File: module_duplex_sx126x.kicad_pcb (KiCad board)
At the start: 4 copper layers, 55.4 x 45.7 mm, 34 parts, among them J1 USB_B_Mini, J2 Conn_01x08_Pin, J3 Conn_01x05, J4 Conn_01x04, J6 Conn_01x02, SW1 SW_Push, U1 STM32F103C8Tx, U2 AMS1117-3.3, U3 SN65HVD230, U4 Ai-Thinker-Ra-02, U5 Ai-Thinker-Ra-02, Y1 16M, Y2 32.768k

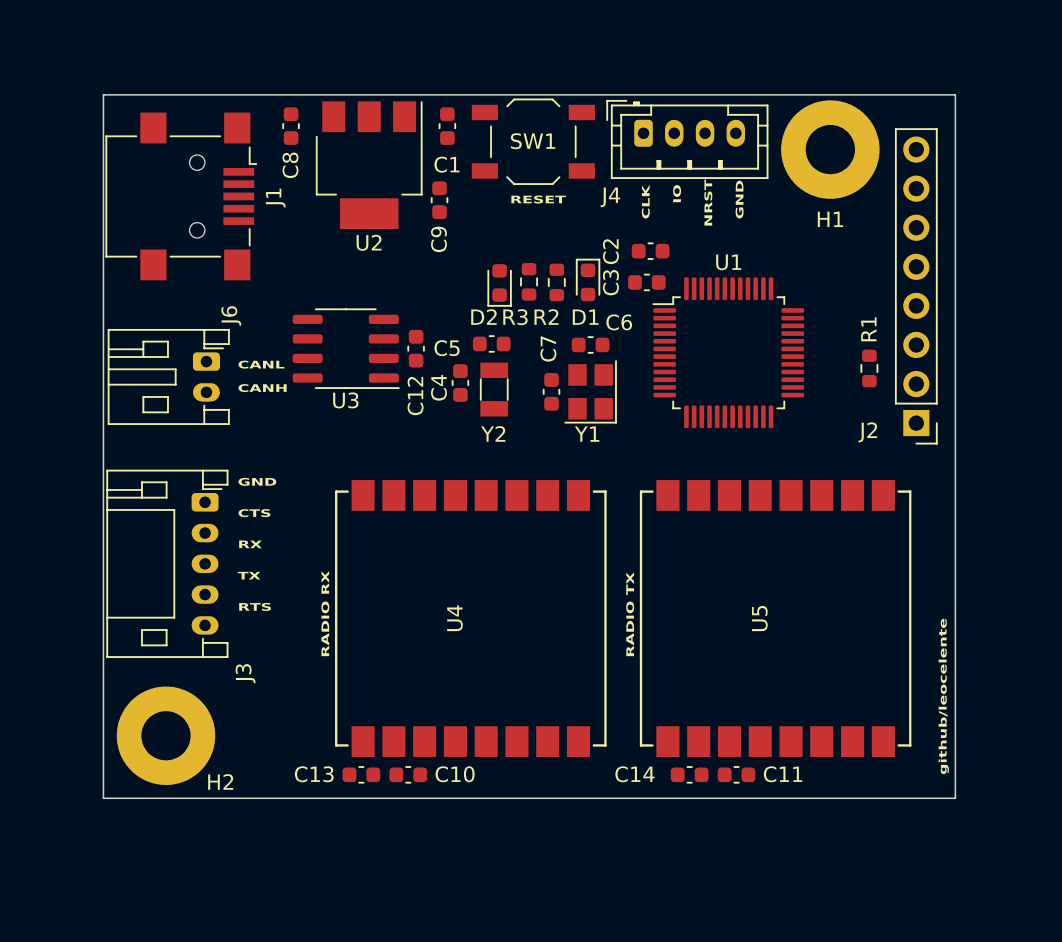
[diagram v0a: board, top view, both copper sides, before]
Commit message: Reduced expansion pins by simplifying select function with pull up/down
Signed-off-by: Leonardo Celente <leocelente@gmail.com>
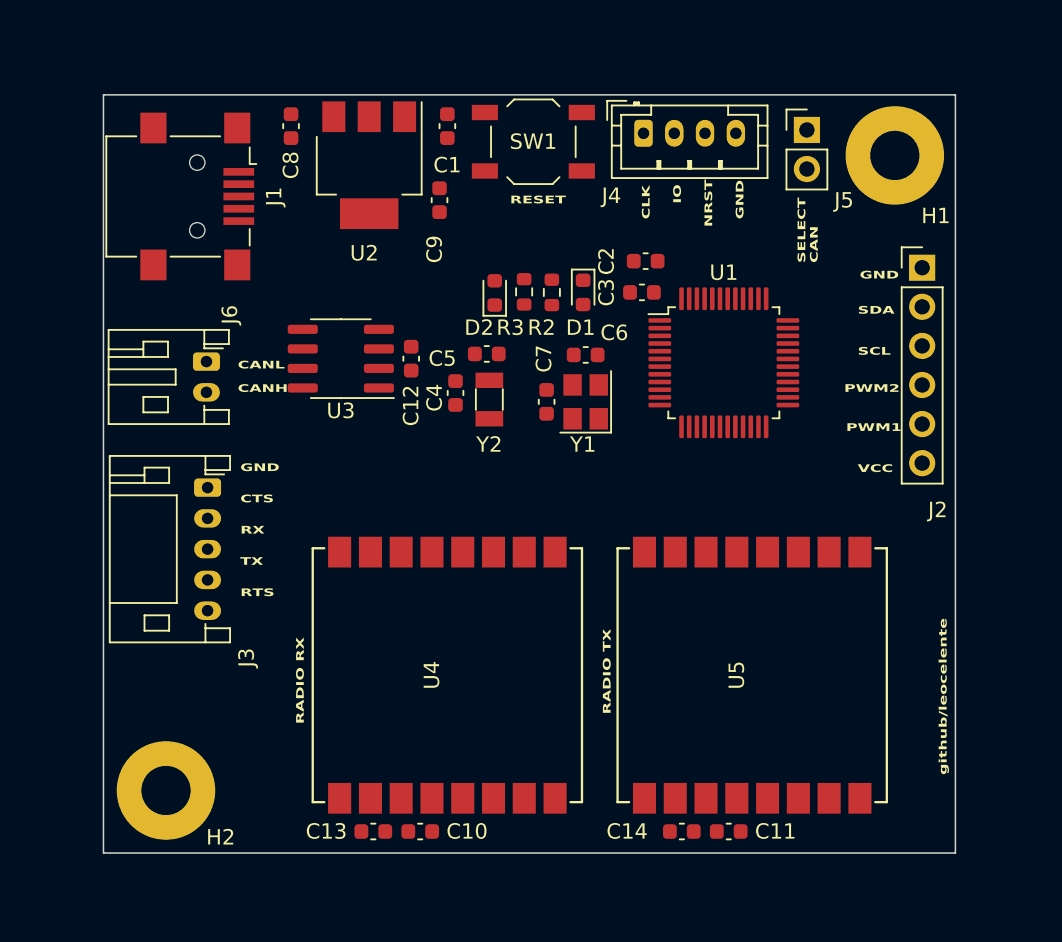
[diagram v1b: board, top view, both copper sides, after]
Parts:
- removed R1: 10k, Resistor_SMD:R_0603_1608Metric
- added J5: Conn_01x02_Pin, Connector_PinHeader_2.54mm:PinHeader_1x02_P2.54mm_Vertical, F.Cu at (108.7, 47.0)
- J2: value Conn_01x08_Pin -> Conn_01x06_Pin; footprint Connector_PinHeader_2.54mm:PinHeader_1x08_P2.54mm_Vertical -> Connector_PinHeader_2.54mm:PinHeader_1x06_P2.54mm_Vertical
- moved J2 10.1 mm to (116.2, 55.9), turned to 0 degrees
- moved H1 4.21 mm to (114.4, 48.6)
- moved U4 3.99 mm to (85.3, 82.4)
- moved U5 3.99 mm to (105.2, 82.4)
- moved C13 3.76 mm to (80.5, 92.6)
- moved C10 3.76 mm to (83.6, 92.6)
- moved C11 3.72 mm to (103.6, 92.6)
- moved C14 3.72 mm to (100.6, 92.6)
- moved H2 3.56 mm to (67.1, 89.9)
- moved J3 0.97 mm to (69.8, 70.2)
- moved C7 0.72 mm to (91.8, 64.7)
- moved Y1 0.72 mm to (94.3, 64.7)
- moved C2 0.72 mm to (98.2, 55.5)
- moved C5 0.72 mm to (87.9, 61.5)
- moved R3 0.72 mm to (90.3, 57.5)
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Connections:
- J2 pad 2: Net-(J2-Pin_2) -> /I2C_SDA
- J2 pad 3: VCC -> /I2C_SCL
- J2 pad 4: /I2C_SDA -> /PWM_2
- J2 pad 5: /I2C_SCL -> /PWM_1
- J2 pad 6: /PWM_2 -> VCC
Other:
- board size 55.4 x 45.7 mm -> 55.4 x 49.3 mm
- board text added: "PWM1"
- board text added: "PWM2"
- board text added: "SCL"
- board text added: "SDA"
- board text added: "SELECT CAN"
- board text added: "VCC"

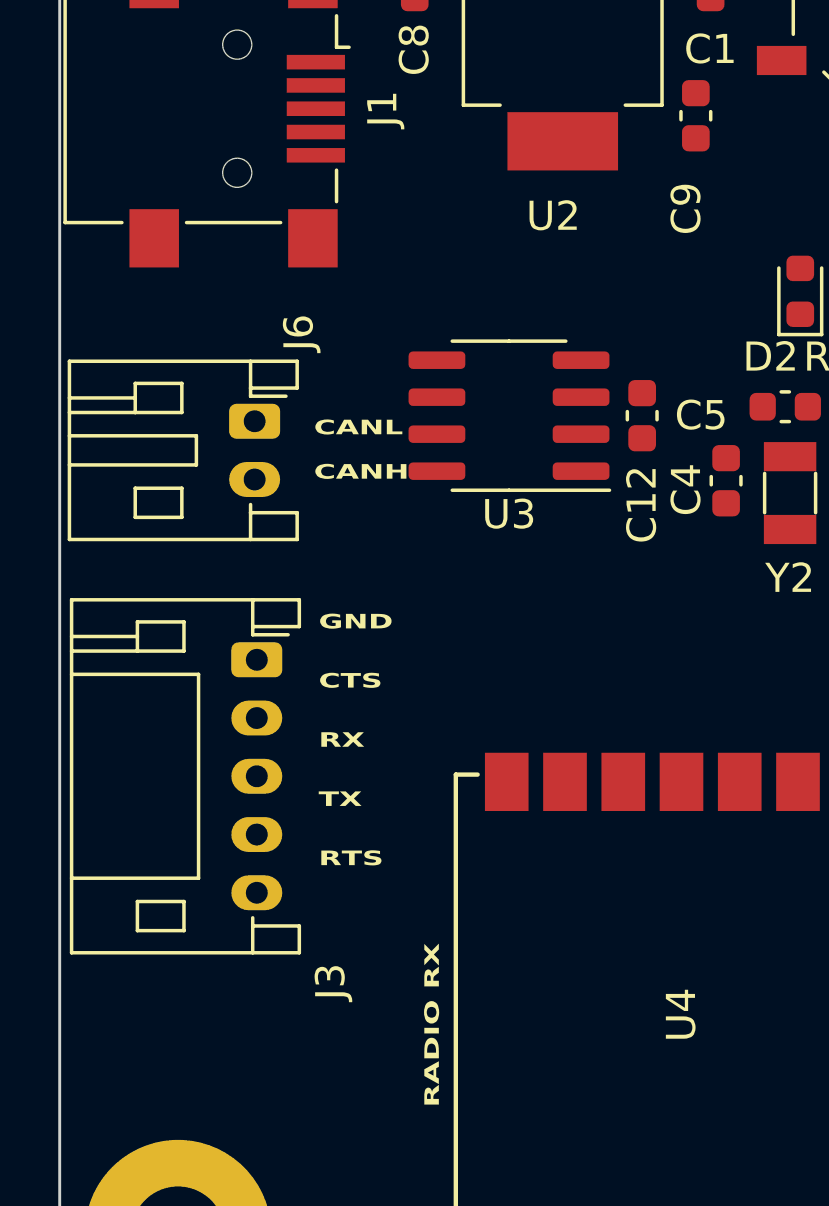
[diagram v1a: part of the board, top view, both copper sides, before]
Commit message: Added USB resistors
Signed-off-by: Leonardo Celente <leocelente@gmail.com>
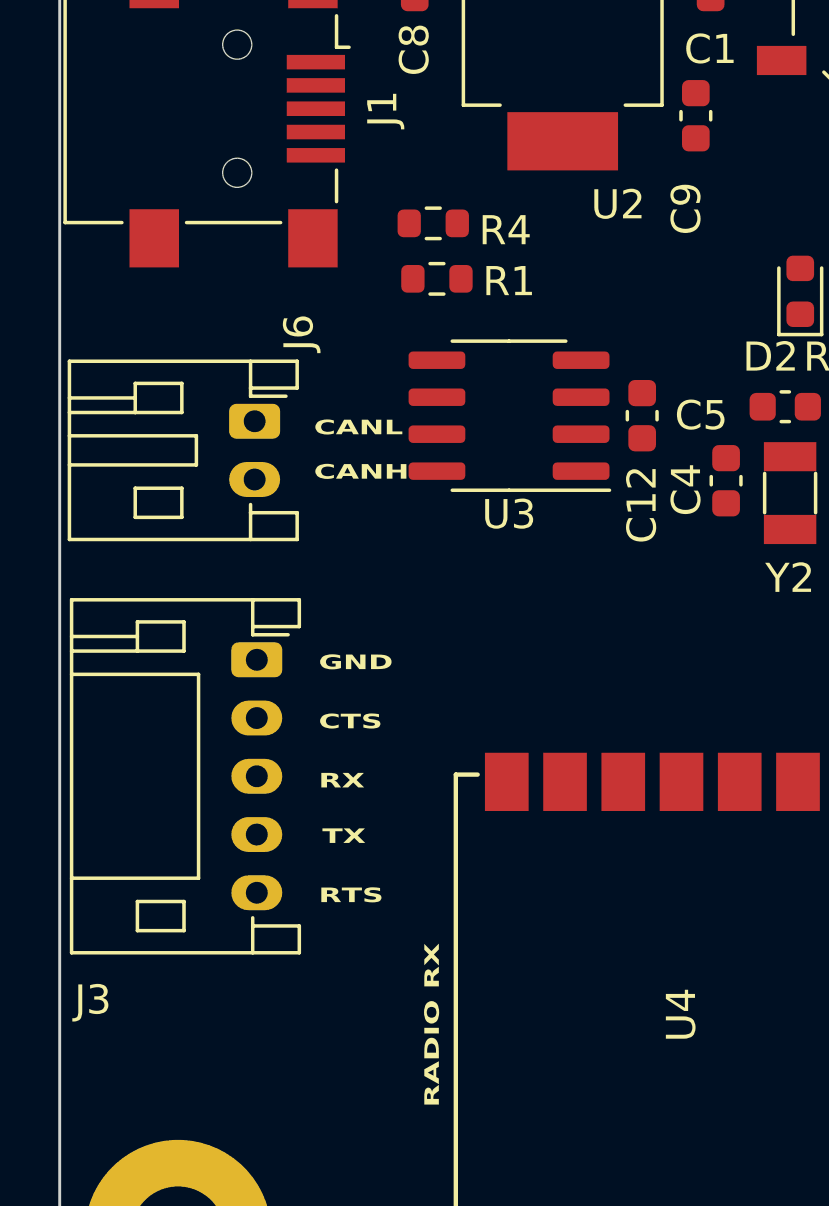
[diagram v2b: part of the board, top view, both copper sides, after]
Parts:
- added R1: 22, Resistor_SMD:R_0603_1608Metric, F.Cu at (75.9, 57.1)
- added R4: 22, Resistor_SMD:R_0603_1608Metric, F.Cu at (75.8, 55.2)
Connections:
- J1 pad 2: /USB_DM -> Net-(J1-D-)
- J1 pad 3: /USB_DP -> Net-(J1-D+)

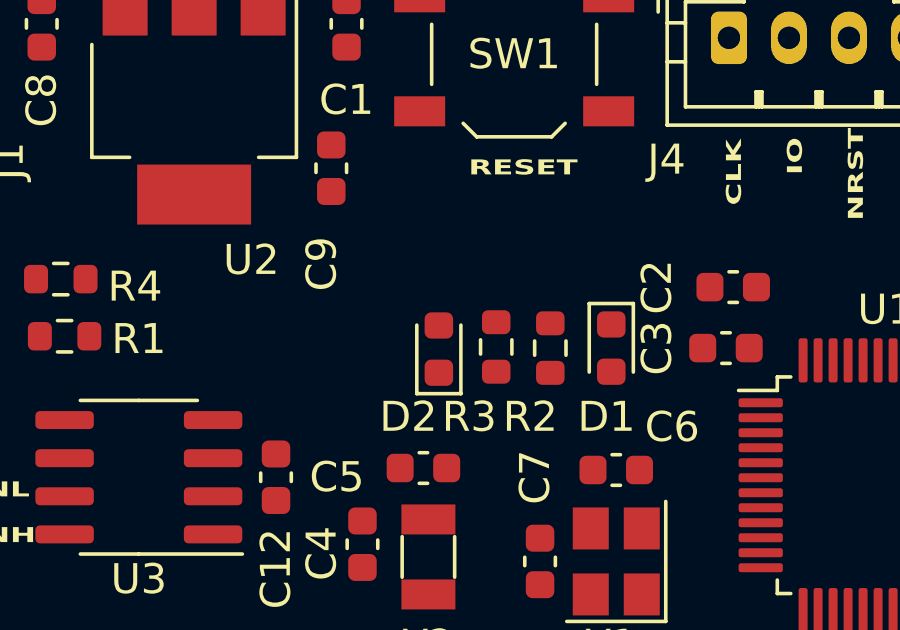
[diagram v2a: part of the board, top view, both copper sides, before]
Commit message: Added power indicator LED
Signed-off-by: Leonardo Celente <leocelente@gmail.com>
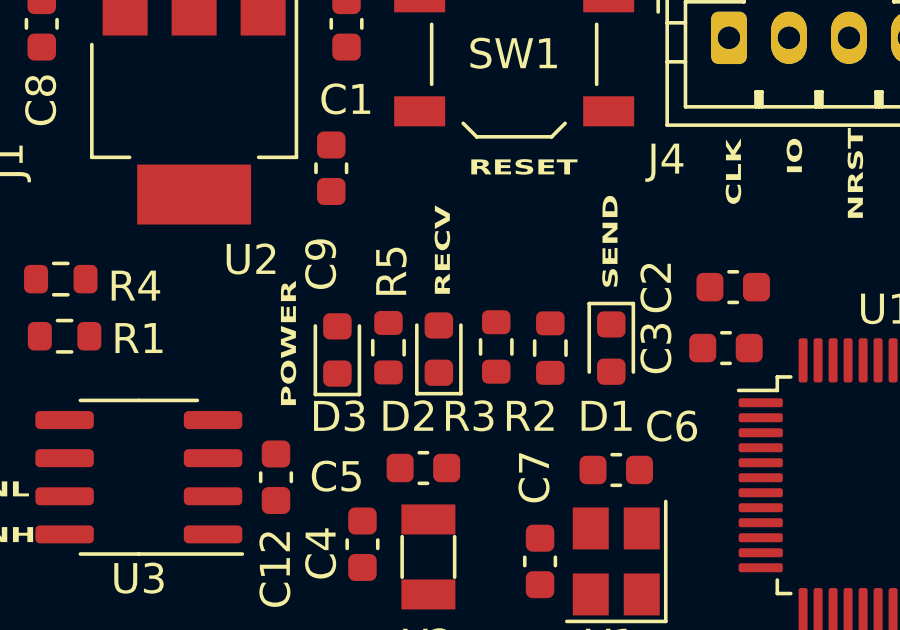
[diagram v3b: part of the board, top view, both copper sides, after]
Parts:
- added D3: LED, LED_SMD:LED_0603_1608Metric, F.Cu at (85.0, 57.6)
- added R5: 330, Resistor_SMD:R_0603_1608Metric, F.Cu at (86.7, 57.5)
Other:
- board text added: "POWER"
- board text added: "RECV"
- board text added: "SEND"
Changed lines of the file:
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@@
   (net 57 "Net-(D2-K)")
   (net 58 "Net-(J1-D+)")
+  (net 59 "Net-(D3-K)")
   (footprint "Connector_JST:JST_PH_S2B-PH-K_1x02_P2.00mm_Horizontal" (layer "F.Cu")
     (at 69.686 62.04 -90)
@@
     (pad "2" smd roundrect (at 0.825 0 90) (size 0.8 0.95) (layers "F.Cu" "F.Paste" "F.Mask") (roundrect_rratio 0.25)
       (net 42 "/RECV_LED") (pintype "passive"))
+    (model "${KICAD6_3DMODEL_DIR}/Resistor_SMD.3dshapes/R_0603_1608Metric.wrl"
+      (offset (xyz 0 0 0))
+      (scale (xyz 1 1 1))
+      (rotate (xyz 0 0 0))
+    )
+  )
+  (footprint "Resistor_SMD:R_0603_1608Metric" (layer "F.Cu")
+    (at 86.741 57.531 90)
+    (descr "Resistor SMD 0603 (1608 Metric), square (rectangular) end terminal, IPC_7351 nominal, (Body size source: IPC-SM-782 page 72, https://www.pcb-3d.com/wordpress/wp-content/uploads/ipc-sm-782a_amendment_1_and_2.pdf), generated with kicad-footprint-generator")
+    (tags "resistor")
+    (property "Sheetfile" "module_duplex_sx126x.kicad_sch")
+    (property "Sheetname" "")
+    (property "ki_description" "Resistor")
+    (property "ki_keywords" "R res resistor")
+    (attr smd)
+    (fp_text reference "R5" (at 2.54 0.127 90) (layer "F.SilkS")
+        (effects (font (size 1 1) (thickness 0.15)))
+    )
+    (fp_text value "330" (at 0 1.43 90) (layer "F.Fab")
+        (effects (font (size 1 1) (thickness 0.15)))
+    )
+    (fp_text user "${REFERENCE}" (at 0 0 90) (layer "F.Fab")
+        (effects (font (size 0.4 0.4) (thickness 0.06)))
+    )
+    (fp_line (start -0.237258 -0.5225) (end 0.237258 -0.5225)
+      (stroke (width 0.12) (type solid)) (layer "F.SilkS"))
+    (fp_line (start -0.237258 0.5225) (end 0.237258 0.5225)
+      (stroke (width 0.12) (type solid)) (layer "F.SilkS"))
+    (fp_line (start -1.48 -0.73) (end 1.48 -0.73)
+      (stroke (width 0.05) (type solid)) (layer "F.CrtYd"))
+    (fp_line (start -1.48 0.73) (end -1.48 -0.73)
+      (stroke (width 0.05) (type solid)) (layer "F.CrtYd"))
+    (fp_line (start 1.48 -0.73) (end 1.48 0.73)
+      (stroke (width 0.05) (type solid)) (layer "F.CrtYd"))
+    (fp_line (start 1.48 0.73) (end -1.48 0.73)
+      (stroke (width 0.05) (type solid)) (layer "F.CrtYd"))
+    (fp_line (start -0.8 -0.4125) (end 0.8 -0.4125)
+      (stroke (width 0.1) (type solid)) (layer "F.Fab"))
+    (fp_line (start -0.8 0.4125) (end -0.8 -0.4125)
+      (stroke (width 0.1) (type solid)) (layer "F.Fab"))
+    (fp_line (start 0.8 -0.4125) (end 0.8 0.4125)
+      (stroke (width 0.1) (type solid)) (layer "F.Fab"))
+    (fp_line (start 0.8 0.4125) (end -0.8 0.4125)
+      (stroke (width 0.1) (type solid)) (layer "F.Fab"))
+    (pad "1" smd roundrect (at -0.825 0 90) (size 0.8 0.95) (layers "F.Cu" "F.Paste" "F.Mask") (roundrect_rratio 0.25)
+      (net 59 "Net-(D3-K)") (pintype "passive"))
+    (pad "2" smd roundrect (at 0.825 0 90) (size 0.8 0.95) (layers "F.Cu" "F.Paste" "F.Mask") (roundrect_rratio 0.25)
+      (net 1 "GND") (pintype "passive"))
     (model "${KICAD6_3DMODEL_DIR}/Resistor_SMD.3dshapes/R_0603_1608Metric.wrl"
       (offset (xyz 0 0 0))
@@
       (net 12 "unconnected-(J1-Shield-Pad6)") (pinfunction "Shield") (pintype "passive+no_connect"))
     (model "${KICAD6_3DMODEL_DIR}/Connector_USB.3dshapes/USB_Mini-B_Lumberg_2486_01_Horizontal.wrl"
+      (offset (xyz 0 0 0))
+      (scale (xyz 1 1 1))
+      (rotate (xyz 0 0 0))
+    )
+  )
+  (footprint "LED_SMD:LED_0603_1608Metric" (layer "F.Cu")
+    (at 85.0392 57.6072 90)
+    (descr "LED SMD 0603 (1608 Metric), square (rectangular) end terminal, IPC_7351 nominal, (Body size source: http://www.tortai-tech.com/upload/download/2011102023233369053.pdf), generated with kicad-footprint-generator")
+    (tags "LED")
+    (property "Sheetfile" "module_duplex_sx126x.kicad_sch")
+    (property "Sheetname" "")
+    (property "ki_description" "Light emitting diode")
+    (property "ki_keywords" "LED diode")
+    (attr smd)
+    (fp_text reference "D3" (at -2.2352 0.0508 180) (layer "F.SilkS")
+        (effects (font (size 1 1) (thickness 0.15)))
+    )
+    (fp_text value "LED" (at 0 1.43 90) (layer "F.Fab")
+        (effects (font (size 1 1) (thickness 0.15)))
+    )
+    (fp_text user "${REFERENCE}" (at 0 0 90) (layer "F.Fab")
+        (effects (font (size 0.4 0.4) (thickness 0.06)))
+    )
+    (fp_line (start -1.485 -0.735) (end -1.485 0.735)
+      (stroke (width 0.12) (type solid)) (layer "F.SilkS"))
+    (fp_line (start -1.485 0.735) (end 0.8 0.735)
+      (stroke (width 0.12) (type solid)) (layer "F.SilkS"))
+    (fp_line (start 0.8 -0.735) (end -1.485 -0.735)
+      (stroke (width 0.12) (type solid)) (layer "F.SilkS"))
+    (fp_line (start -1.48 -0.73) (end 1.48 -0.73)
+      (stroke (width 0.05) (type solid)) (layer "F.CrtYd"))
+    (fp_line (start -1.48 0.73) (end -1.48 -0.73)
+      (stroke (width 0.05) (type solid)) (layer "F.CrtYd"))
+    (fp_line (start 1.48 -0.73) (end 1.48 0.73)
+      (stroke (width 0.05) (type solid)) (layer "F.CrtYd"))
+    (fp_line (start 1.48 0.73) (end -1.48 0.73)
+      (stroke (width 0.05) (type solid)) (layer "F.CrtYd"))
+    (fp_line (start -0.8 -0.1) (end -0.8 0.4)
+      (stroke (width 0.1) (type solid)) (layer "F.Fab"))
+    (fp_line (start -0.8 0.4) (end 0.8 0.4)
+      (stroke (width 0.1) (type solid)) (layer "F.Fab"))
+    (fp_line (start -0.5 -0.4) (end -0.8 -0.1)
+      (stroke (width 0.1) (type solid)) (layer "F.Fab"))
+    (fp_line (start 0.8 -0.4) (end -0.5 -0.4)
+      (stroke (width 0.1) (type solid)) (layer "F.Fab"))
+    (fp_line (start 0.8 0.4) (end 0.8 -0.4)
+      (stroke (width 0.1) (type solid)) (layer "F.Fab"))
+    (pad "1" smd roundrect (at -0.7875 0 90) (size 0.875 0.95) (layers "F.Cu" "F.Paste" "F.Mask") (roundrect_rratio 0.25)
+      (net 59 "Net-(D3-K)") (pinfunction "K") (pintype "passive"))
+    (pad "2" smd roundrect (at 0.7875 0 90) (size 0.875 0.95) (layers "F.Cu" "F.Paste" "F.Mask") (roundrect_rratio 0.25)
+      (net 3 "VCC") (pinfunction "A") (pintype "passive"))
+    (model "${KICAD6_3DMODEL_DIR}/LED_SMD.3dshapes/LED_0603_1608Metric.wrl"
       (offset (xyz 0 0 0))
       (scale (xyz 1 1 1))
@@
     (effects (font (size 0.5 0.75) (thickness 0.125) bold) (justify left bottom))
   )
+  (gr_text "SEND" (at 94.4372 55.5752 90) (layer "F.SilkS")
+    (effects (font (size 0.5 0.75) (thickness 0.125) bold) (justify left bottom))
+  )
   (gr_text "RADIO RX" (at 76.073 85.598 90) (layer "F.SilkS")
     (effects (font (size 0.5 0.75) (thickness 0.125) bold) (justify left bottom))
@@
     (effects (font (size 0.5 0.75) (thickness 0.125) bold) (justify left bottom))
   )
+  (gr_text "RECV" (at 88.8492 55.8292 90) (layer "F.SilkS")
+    (effects (font (size 0.5 0.75) (thickness 0.125) bold) (justify left bottom))
+  )
   (gr_text "CTS" (at 71.882 72.644) (layer "F.SilkS")
     (effects (font (size 0.5 0.75) (thickness 0.125) bold) (justify left bottom))
@@
     (effects (font (size 0.5 0.75) (thickness 0.125) bold) (justify left bottom))
   )
+  (gr_text "POWER" (at 83.7184 59.5376 90) (layer "F.SilkS")
+    (effects (font (size 0.5 0.75) (thickness 0.125) bold) (justify left bottom))
+  )

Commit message: First Pass routing top copper layer
Signed-off-by: Leonardo Celente <leocelente@gmail.com>
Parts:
- moved R3 22.6 mm to (112.9, 56.8)
- moved D2 22.1 mm to (110.5, 56.1), turned to 180 degrees
- moved R2 21.1 mm to (112.9, 53.7)
- moved D3 20.1 mm to (64.9, 58.5), turned to 180 degrees
- moved R5 18.5 mm to (68.3, 58.4), turned to 0 degrees
- moved D1 17.0 mm to (110.5, 52.9), turned to 180 degrees
- moved C12 2.91 mm to (81.8, 64.5), turned to -90 degrees
- moved R4 2.12 mm to (77.9, 55.3)
- moved U3 1.76 mm to (78.3, 63.6), turned to -90 degrees
- moved U4 1.20 mm to (84.2, 82.3)
- moved C13 1.08 mm to (79.5, 92.6)
- moved C10 1.08 mm to (82.5, 92.6)
- moved C2 1.06 mm to (97.7, 56.5)
- moved R1 0.84 mm to (76.8, 56.9)
- moved C7 0.64 mm to (91.4, 64.1)
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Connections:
- net /USB_DM renamed /USB_DN
- net Net-(J1-D+) renamed /CONN_DP
- net Net-(J1-D-) renamed /CONN_DN
- J3 pad 3: /UART_RX -> /UART_RTS
- J3 pad 5: /UART_RTS -> /UART_RX
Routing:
- net /USB_DP: track 0.00 -> 38.0 mm
- net /USB_DN: track 0.00 -> 37.7 mm
- net /UART_RX: track 0.00 -> 35.8 mm
- net /RADIO_SEND_DIO1: track 0.00 -> 35.4 mm
- net /UART_TX: track 0.00 -> 35.4 mm
- net /RADIO_SEND_DIO0: track 0.00 -> 35.3 mm
- net /RADIO_SEND_RST: track 0.00 -> 35.2 mm
- net /UART_RTS: track 0.00 -> 34.5 mm
- net /RADIO_RECV_RST: track 0.00 -> 34.3 mm
- net /UART_CTS: track 0.00 -> 33.9 mm
- net /RADIO_RECV_DIO0: track 0.00 -> 33.7 mm
- net /RADIO_RECV_DIO1: track 0.00 -> 33.1 mm
- net /CAN_RX: track 0.00 -> 30.7 mm
- net /RADIO_RECV_MOSI: track 0.00 -> 30.1 mm
- net /RADIO_SEND_MOSI: track 0.00 -> 29.3 mm
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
